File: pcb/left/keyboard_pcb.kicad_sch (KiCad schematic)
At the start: 51 parts, among them J1 TRRS, K0 KEYSW, K1 KEYSW, K10 KEYSW, K11 KEYSW, K12 KEYSW, K13 KEYSW, K14 KEYSW, K15 KEYSW, K2 KEYSW, K20 KEYSW, K21 KEYSW, K22 KEYSW, K23 KEYSW, K24 KEYSW, K25 KEYSW, K3 KEYSW, K30 KEYSW, K31 KEYSW, K32 KEYSW, K4 KEYSW, K5 KEYSW, U1 MCP23009-E/SO, U2 Pico

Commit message: Revision 1.1 WIP; left pcb -RFR-
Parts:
- U2: footprint RPi_Pico:RPi_Pico_SMD_TH -> misc:RPi_Pico_SMD_TH
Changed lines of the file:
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@@
       (effects (font (size 1.27 1.27)))
     )
-    (property "Footprint" "RPi_Pico:RPi_Pico_SMD_TH" (at 50.8 53.34 90)
+    (property "Footprint" "misc:RPi_Pico_SMD_TH" (at 50.8 53.34 90)
       (effects (font (size 1.27 1.27)) hide)
     )

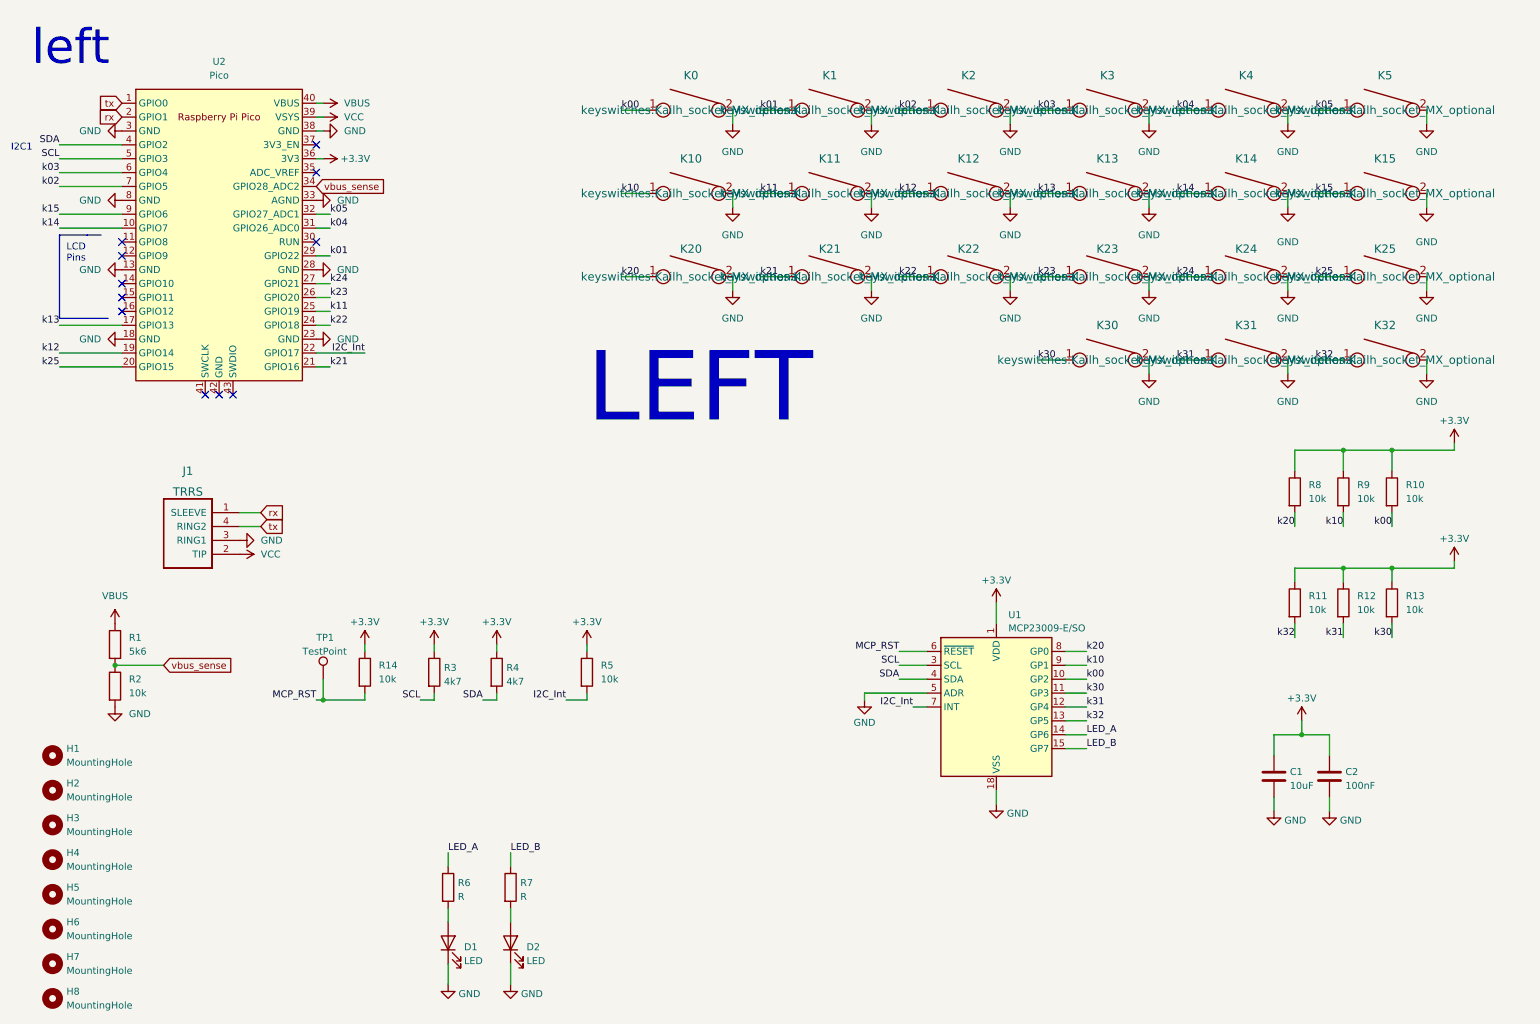
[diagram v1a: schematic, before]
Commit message: Revision 1.1 -RFR- new standoff holes added and left/right pcb positions synced
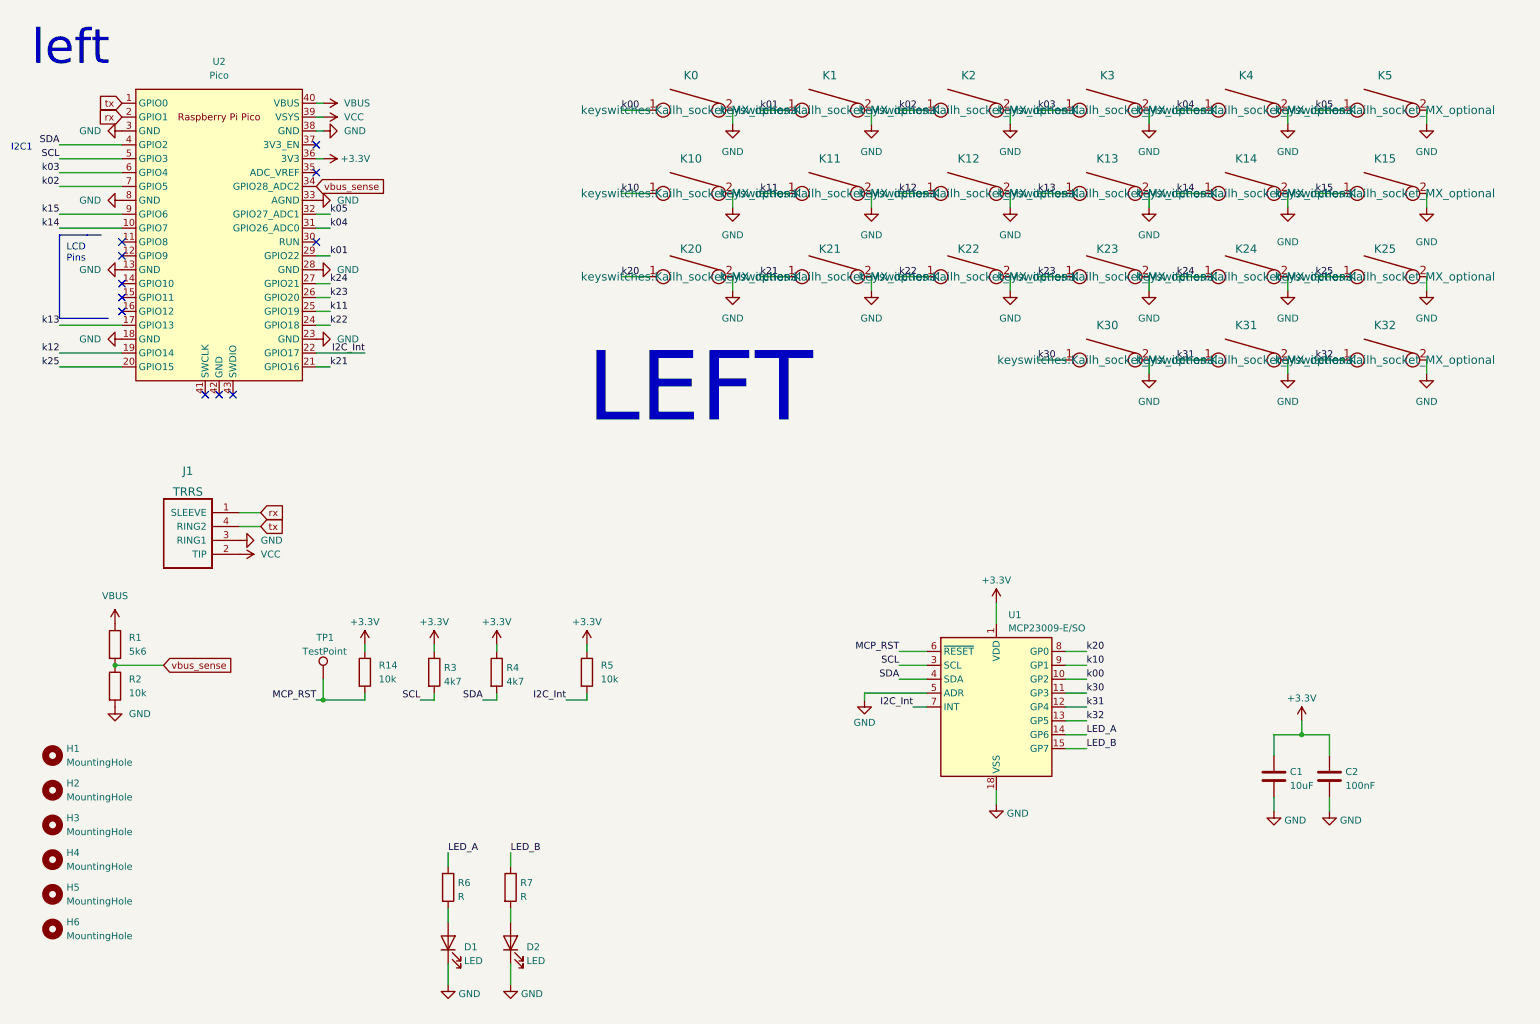
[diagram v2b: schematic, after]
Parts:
- removed H7, H8: MountingHole, misc:MountingHole_2.2mm_M2-8mm, symbol Mechanical:MountingHole
- removed R10, R11, R12, R13, R8, R9: 10k, Resistor_SMD:R_0603_1608Metric_Pad0.98x0.95mm_HandSolder, symbol Device:R
- H1, H2, H3, H4, H5, H6: footprint misc:MountingHole_2.2mm_M2-8mm -> misc:MountingHole_3.7mm_Pad_TopBottom

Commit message: Revision 1.1 -RFR- right pcb layout fix added Standoff PN
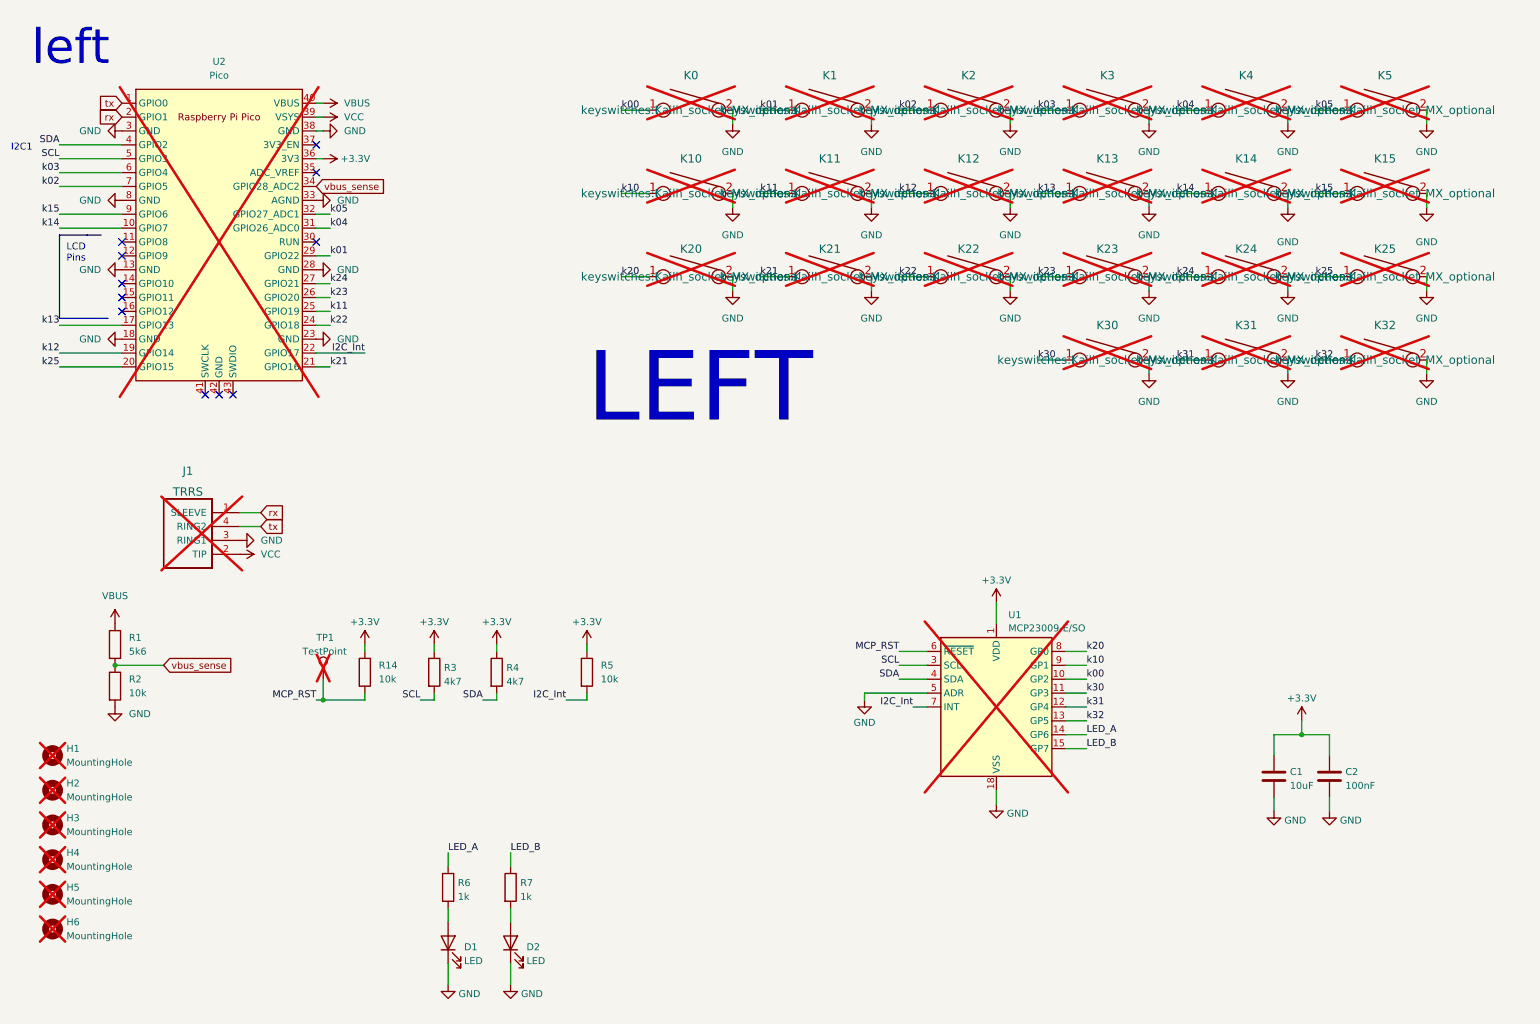
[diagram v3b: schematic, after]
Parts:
- C1: LCSC (none) -> C19702
- C2: LCSC (none) -> C14663
- D1, D2: LCSC (none) -> C72038
- H1, H2, H3, H4, H5, H6, J1, K0, K1, K10, K11, K12, K13, K14, K15, K2, K20, K21, K22, K23, K24, K25, K3, K30, K31, K32, K4, K5, TP1, U1, U2: now not fitted
- R1: LCSC (none) -> C114627
- R14, R2, R5: LCSC (none) -> C23192
- R3, R4: LCSC (none) -> C99782
- R6, R7: value R -> 1k; LCSC (none) -> C100050
